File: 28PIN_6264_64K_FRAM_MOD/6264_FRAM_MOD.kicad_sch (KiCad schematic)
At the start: 13 parts, among them J1 Conn_01x02, U1 TL431DBZ, U10 TC5564APL_Adapter, U2 74AHC2G00, U3 FM16W08

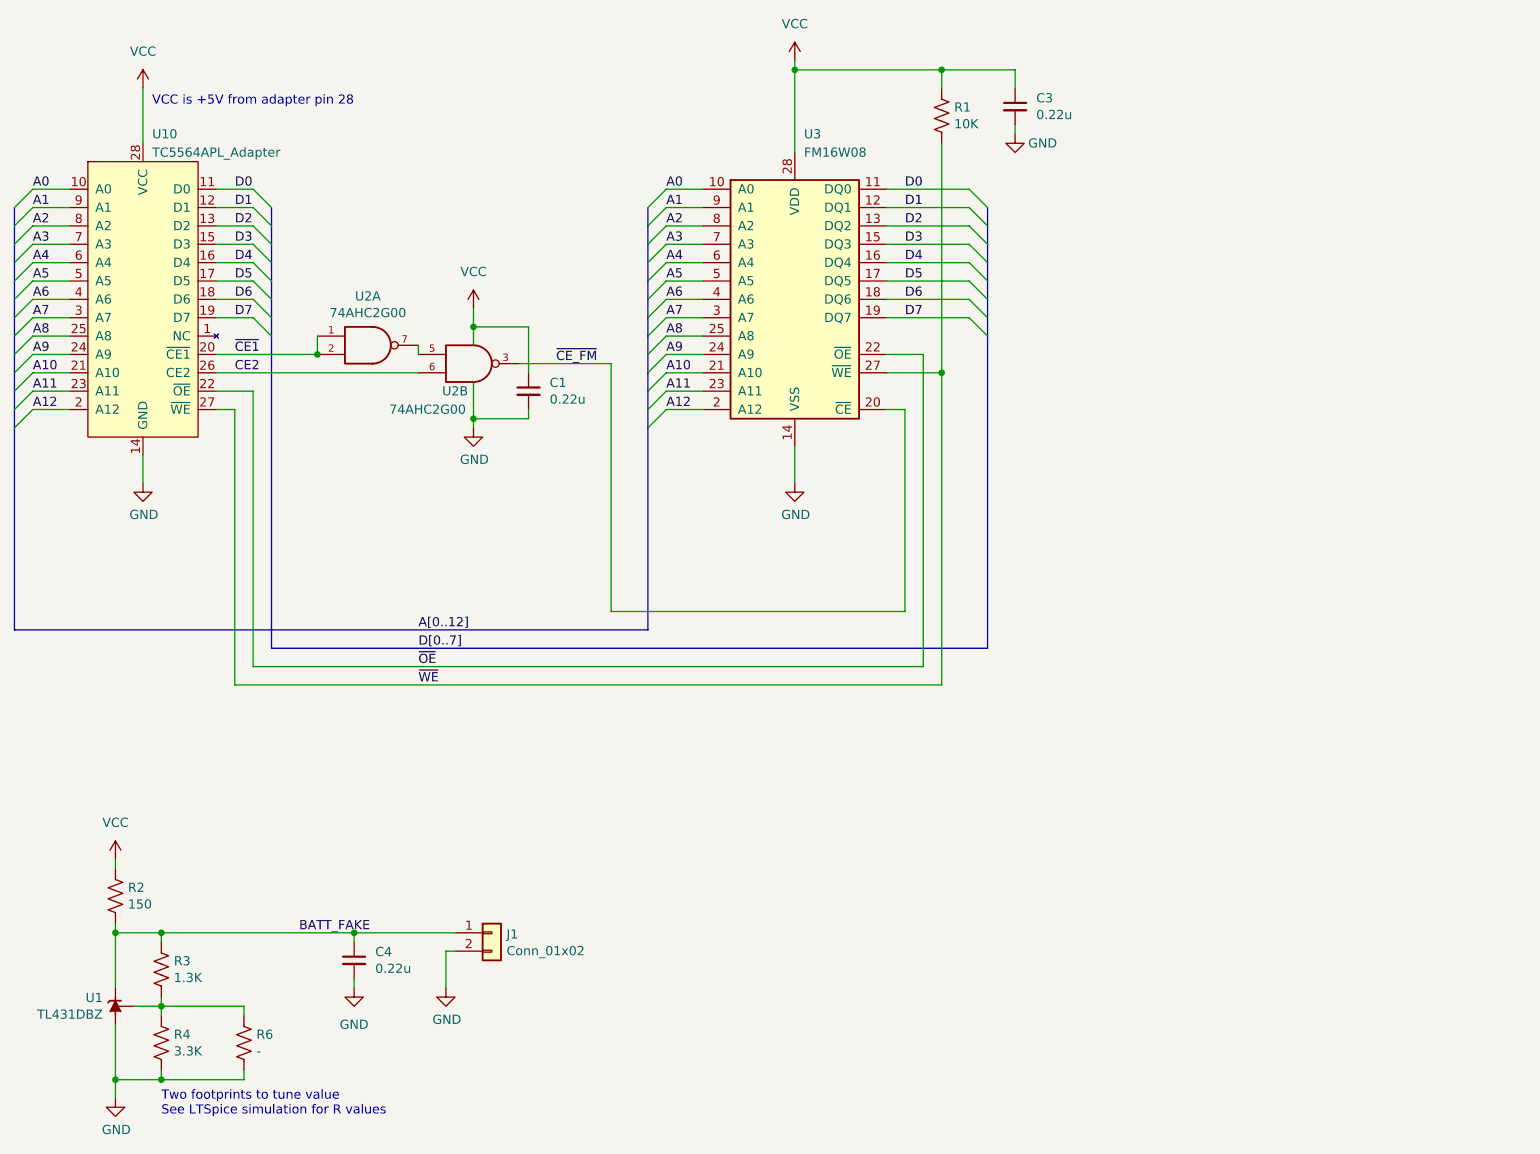
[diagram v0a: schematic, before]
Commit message: Updated to KiCAD 7 and library updates.
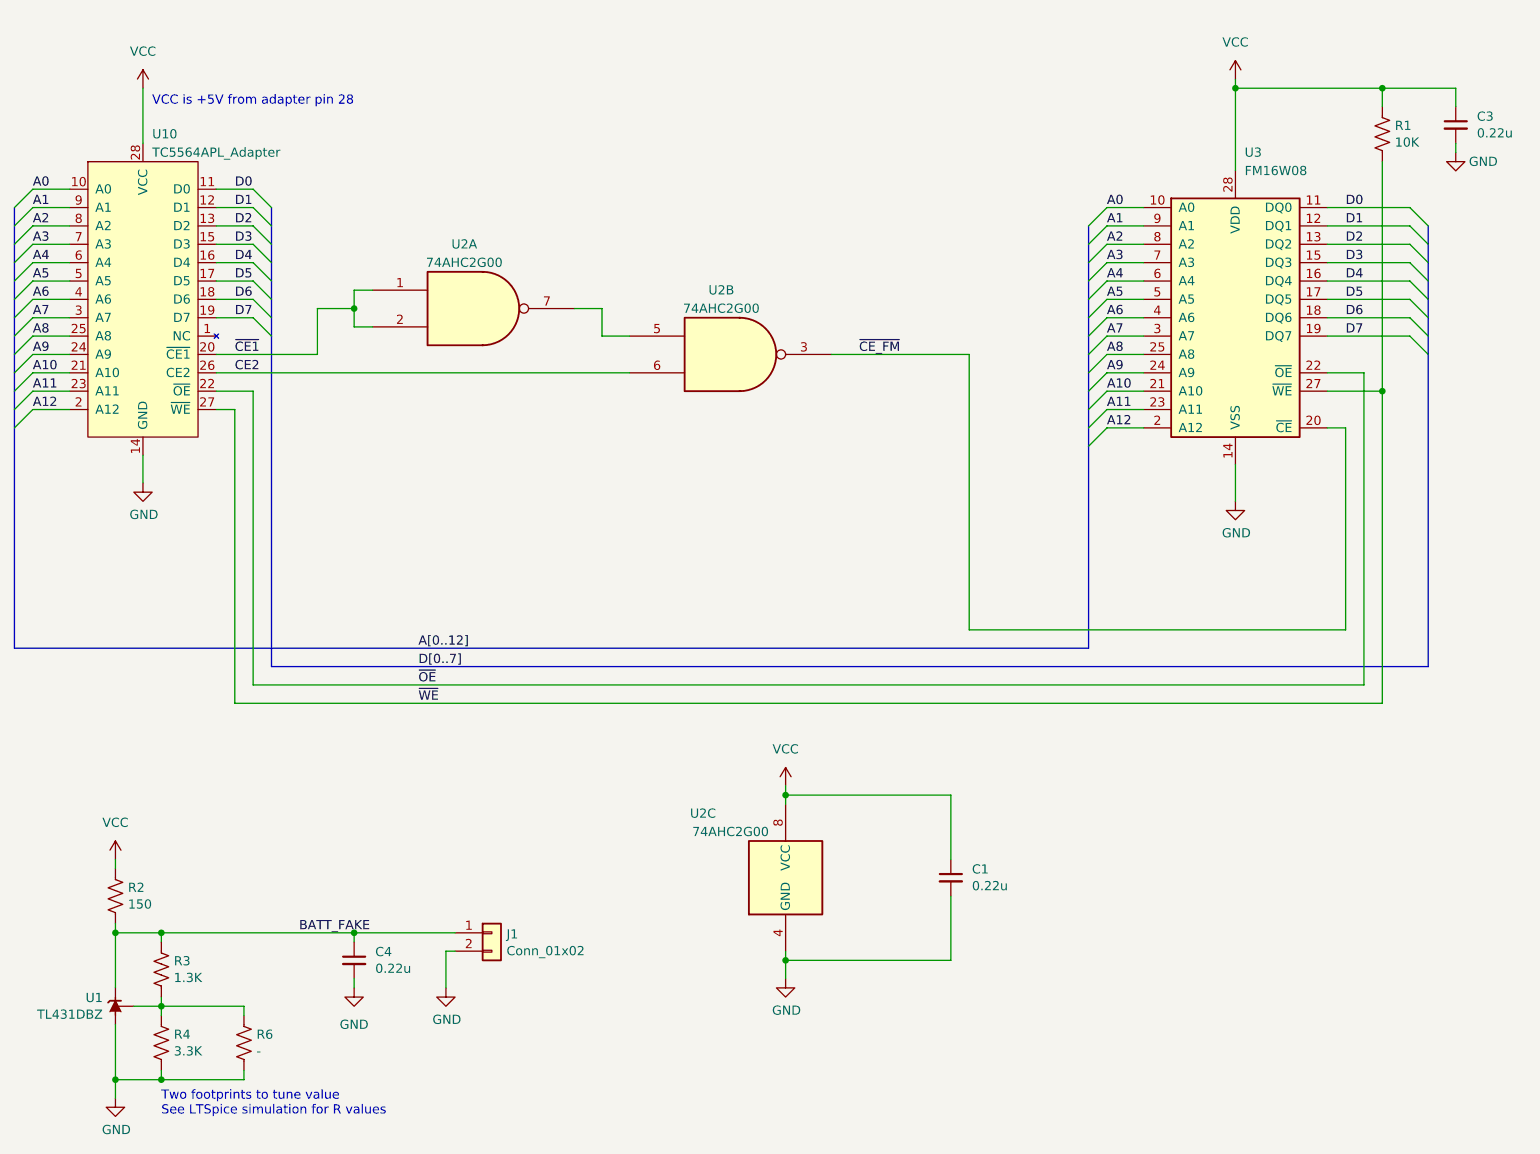
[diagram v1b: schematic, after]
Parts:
- added unit 3 of U2
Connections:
- net GND: now also U2.4 (GND); no longer U2.4 (GND), U2.4 (GND)
- net VCC: now also U2.8 (VCC); no longer U2.8 (VCC), U2.8 (VCC)
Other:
- moved on the sheet: C1, C3, R1, U3
